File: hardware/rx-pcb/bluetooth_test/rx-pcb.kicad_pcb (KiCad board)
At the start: 4 copper layers, 23.1 x 37.6 mm, 36 parts, among them J1 Conn_01x05_Pin, J2 Conn_01x04_Pin, J3 Conn_Coaxial_Small, J4 Conn_01x04_Pin, J5 Conn_01x02_Pin, SW1 SW_SPST, U1 STM32WB05KZV6TR, U2 STS4L-AD1B-R3, U3 LMT70AYFQR, X1 Q22FA12800025, X2 ABS07-32.768KHZ-1-T

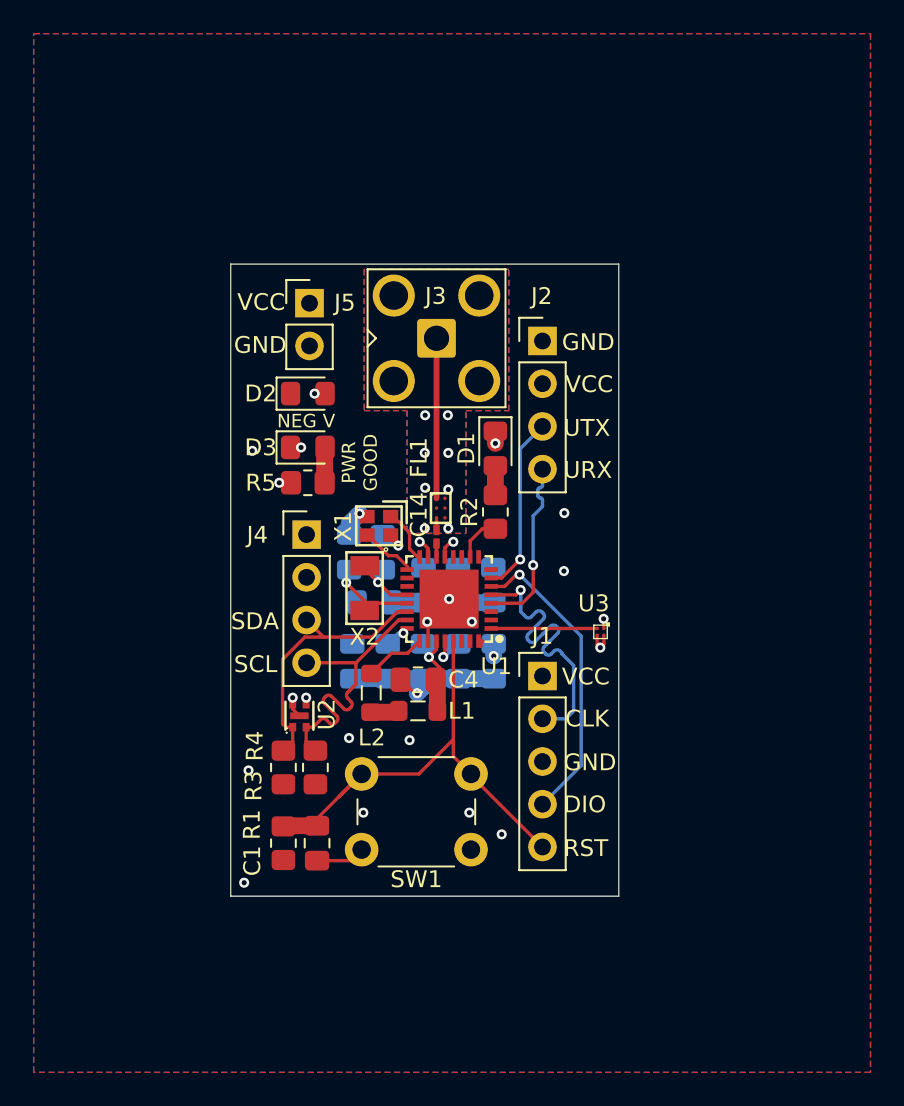
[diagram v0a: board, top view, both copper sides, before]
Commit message: backup of sensor-bluetooth board. re-wiring it.
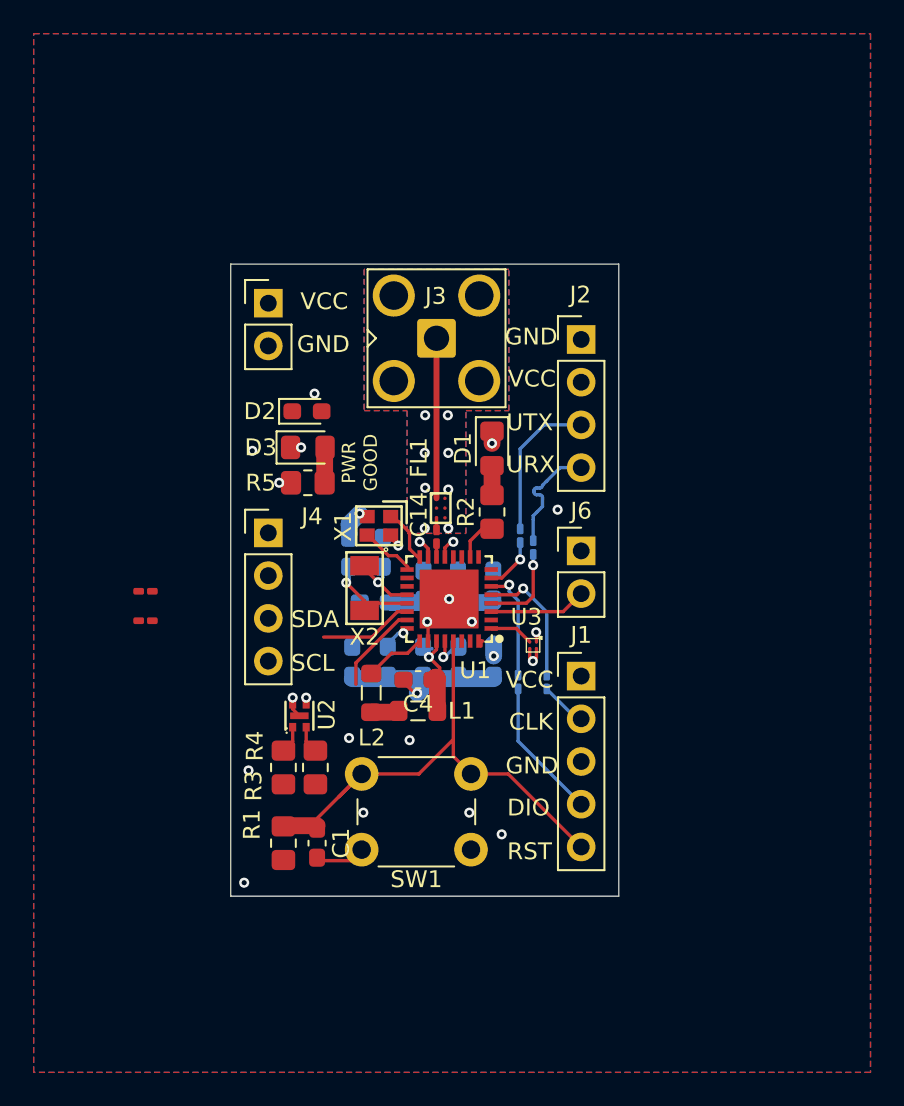
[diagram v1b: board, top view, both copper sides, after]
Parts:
- added J6: Conn_01x02_Pin, Connector_PinHeader_2.54mm:PinHeader_1x02_P2.54mm_Vertical, F.Cu at (163.1, 98.8)
- added R1: 0, Resistor_SMD:R_0201_0603Metric_Pad0.64x0.40mm_HandSolder, F.Cu at (137.2, 101.2)
- added R10: 0, Resistor_SMD:R_0201_0603Metric_Pad0.64x0.40mm_HandSolder, B.Cu at (160.2, 98.5)
- added R6: 0, Resistor_SMD:R_0201_0603Metric_Pad0.64x0.40mm_HandSolder, F.Cu at (137.2, 102.9)
- added R7: 0, Resistor_SMD:R_0201_0603Metric_Pad0.64x0.40mm_HandSolder, B.Cu at (159.4, 97.8)
- added R8: 0, Resistor_SMD:R_0201_0603Metric_Pad0.64x0.40mm_HandSolder, B.Cu at (159.3, 106.5)
- added R9: 0, Resistor_SMD:R_0201_0603Metric_Pad0.64x0.40mm_HandSolder, B.Cu at (161.0, 106.5)
- C1, C10, C11, C12, C13, C2, C3, C4, C5, C6, C7, C8, C9: footprint rx-parts:C_0805_2012Metric_Pad1.18x1.45mm_HandSolder -> Capacitor_SMD:C_0603_1608Metric_Pad1.08x0.95mm_HandSolder
- D2: value LED -> D_Zener; footprint rx-parts:LED_0805_2012Metric_Pad1.15x1.40mm_HandSolder -> Diode_SMD:D_0603_1608Metric_Pad1.05x0.95mm_HandSolder
- R3, R4: value 100k -> 50k
- moved U3 4.09 mm to (160.2, 104.4)
- moved J5 2.45 mm to (144.4, 84.0)
- moved J2 2.30 mm to (163.1, 86.2)
- moved J1 2.30 mm to (163.1, 106.2)
- moved J4 2.28 mm to (144.4, 97.7)
- moved D2 1.05 mm to (146.8, 90.5)
- moved D1 0.20 mm to (157.8, 92.7)
- moved R2 0.20 mm to (157.8, 96.4)
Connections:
- U1 pad 22: /i2c_sda -> Net-(U1-PB7)
- U1 pad 23: /i2c_scl -> Net-(U1-PB6)
- U1 pad 3: unconnected-(U1-PB1-Pad3) -> /ADC_jump
- U1 pad 4: /uart_rx -> Net-(U1-PB0)
- U1 pad 5: /swclk -> Net-(U1-PA3)
- U1 pad 6: /swdio -> Net-(U1-PA2)
- U1 pad 7: /uart_tx -> Net-(U1-PA1)
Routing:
- net /i2c_scl: track 17.6 -> 1.62 mm
- net /swclk: track 18.0 -> 2.78 mm, vias 1 -> 0
- net /i2c_sda: track 16.2 -> 1.62 mm
- net /swdio: track 18.1 -> 8.41 mm, vias 1 -> 0
- net Net-(U1-PA3): track 0.00 -> 7.79 mm, vias 0 -> 1
- net Net-(U1-PA2): track 0.00 -> 6.72 mm, vias 0 -> 1
- net /ADC_jump: track 0.00 -> 5.79 mm
- net Net-(U1-PB7): track 0.00 -> 5.59 mm
- net Net-(U1-PB6): track 0.00 -> 5.37 mm
- net Net-(U1-PB0): track 0.00 -> 5.17 mm, vias 0 -> 1
- net /TMP_A: track 6.30 -> 2.62 mm
- net /uart_rx: track 10.6 -> 6.97 mm, vias 1 -> 0
- net Net-(U1-PA1): track 0.00 -> 3.18 mm, vias 0 -> 1
- net /rst: track 29.0 -> 31.3 mm
- net /uart_tx: track 10.6 -> 8.98 mm, vias 1 -> 0
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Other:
- board text removed: "NEG V"

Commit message: updated rx-board with compartmentalization resistors, updated silkscreen
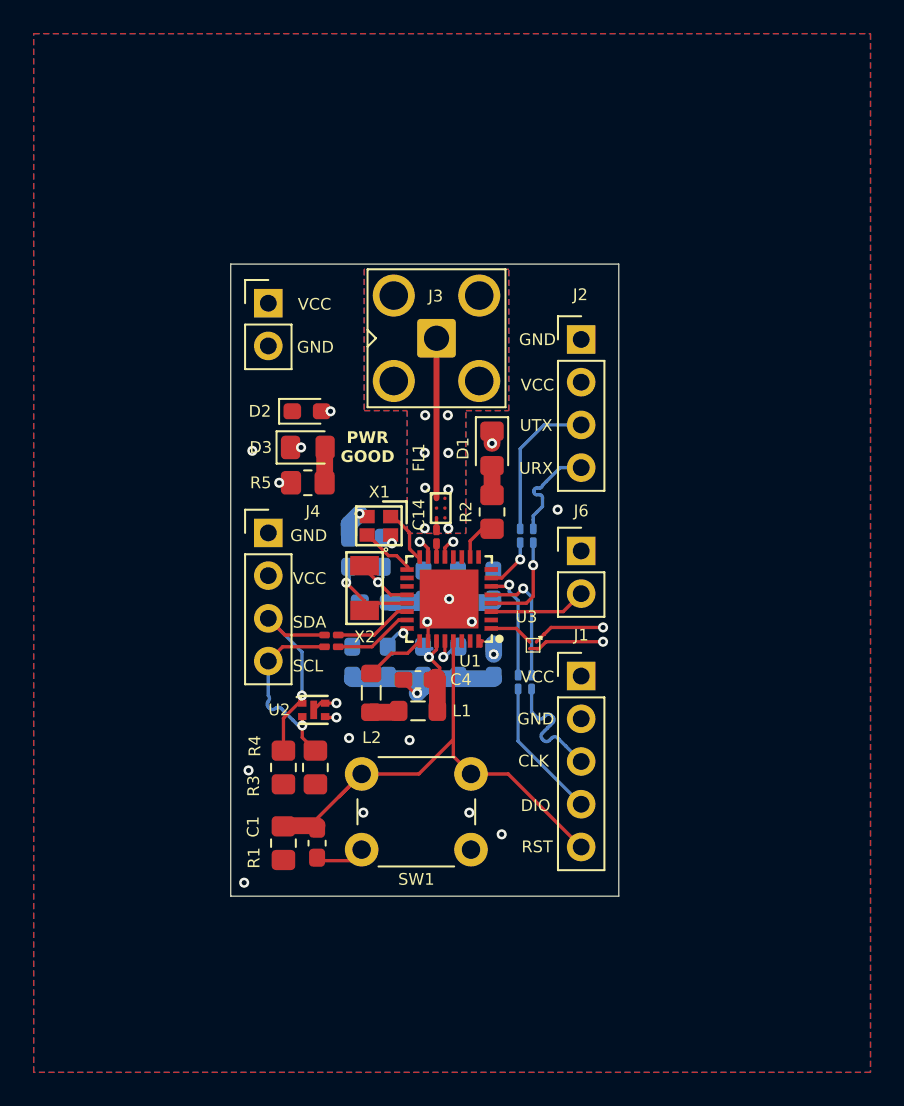
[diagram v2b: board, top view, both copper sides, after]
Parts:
- moved R1 11.5 mm to (148.2, 104.5), turned to 180 degrees
- moved R6 11.1 mm to (148.2, 103.8)
- moved U2 0.92 mm to (147.2, 108.2), turned to 0 degrees
- moved R9 0.90 mm to (160.1, 106.5)
- moved R10 0.70 mm to (160.2, 97.8)
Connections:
- J1 pad 2: /swclk -> GND
- J1 pad 3: GND -> /swclk
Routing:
- net /i2c_sda: track 1.62 -> 13.0 mm, vias 0 -> 1
- net /i2c_scl: track 1.62 -> 11.4 mm, vias 0 -> 1
- net /swclk: track 2.78 -> 7.62 mm
- net GND: track 26.1 -> 30.5 mm
- net VCC: track 6.78 -> 10.4 mm
- net Net-(U1-PB7): track 5.59 -> 4.67 mm
- net Net-(U1-PB0): track 5.17 -> 5.87 mm
- net /uart_rx: track 6.97 -> 6.27 mm
- net Net-(U1-PB6): track 5.37 -> 4.75 mm

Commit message: updates for dr weeks
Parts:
- removed D3: LED, rx-parts:LED_0805_2012Metric_Pad1.15x1.40mm_HandSolder
- removed J6: Conn_01x02_Pin, Connector_PinHeader_2.54mm:PinHeader_1x02_P2.54mm_Vertical
- removed the R1 at (148.2, 104.5)
- removed the R1 at (145.3, 116.1)
- removed R5: 10k, rx-parts:R_0805_2012Metric_Pad1.20x1.40mm_HandSolder
- added R1: 0, Resistor_SMD:R_0805_2012Metric_Pad1.20x1.40mm_HandSolder, F.Cu at (164.0, 97.2)
- C1, C4: footprint Capacitor_SMD:C_0603_1608Metric_Pad1.08x0.95mm_HandSolder -> Capacitor_SMD:C_0805_2012Metric_Pad1.18x1.45mm_HandSolder; moved to B.Cu
- C10, C11, C12, C13, C2, C3, C5, C6, C7, C8, C9: footprint Capacitor_SMD:C_0603_1608Metric_Pad1.08x0.95mm_HandSolder -> Capacitor_SMD:C_0805_2012Metric_Pad1.18x1.45mm_HandSolder
- D2, R3, R4: moved to B.Cu
- J3: footprint rx-parts:SMA_Amphenol_901-143_Horizontal -> Connector_Coaxial:SMA_Samtec_SMA-J-P-H-ST-EM1_EdgeMount
- R10, R7, R8, R9: moved to F.Cu
- R6: footprint Resistor_SMD:R_0201_0603Metric_Pad0.64x0.40mm_HandSolder -> Resistor_SMD:R_0805_2012Metric_Pad1.20x1.40mm_HandSolder
- U3: value LMT70AYFQR -> STS4L-AD1B-R3; footprint rx-parts:DSBGA-4_L0.8-W0.8-R2-C2-P0.40-BL -> rx-parts:DFN-4_L1.5-W1.5-P0.80-TL-EP
- moved J2 33.1 mm to (143.2, 112.7), turned to 180 degrees
- moved SW1 31.4 mm to (150.2, 85.7), turned to 0 degrees
- moved C1 28.6 mm to (151.9, 87.9), turned to 90 degrees
- moved R4 28.2 mm to (162.7, 89.4)
- moved U2 27.4 mm to (168.0, 90.4)
- moved J3 26.9 mm to (160.0, 112.4), turned to -90 degrees
- moved J4 26.1 mm to (167.8, 86.0), turned to -90 degrees
- moved R3 25.7 mm to (160.2, 89.4)
- moved J1 24.8 mm to (143.2, 91.4)
- moved D1 19.7 mm to (154.6, 112.1), turned to 90 degrees
- moved R6 19.1 mm to (166.1, 97.2), turned to -90 degrees
- moved C3 17.3 mm to (166.5, 100.2)
- moved C2 16.2 mm to (166.2, 105.0), turned to -90 degrees
- moved C11 15.9 mm to (163.5, 98.0), turned to 0 degrees
- moved X2 15.6 mm to (165.7, 102.6), turned to 90 degrees
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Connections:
- U1 pad 3: /ADC_jump -> unconnected-(U1-PB1-Pad3)
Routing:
- net /i2c_scl: track 11.4 -> 21.0 mm, vias 1 -> 4
- net GND: track 30.5 -> 22.8 mm, vias 22 -> 38
- net /rst: track 31.3 -> 38.1 mm, vias 0 -> 1
- net /ANT: track 9.52 -> 3.38 mm
- net VCC: track 10.4 -> 4.60 mm, vias 13 -> 16
- net /ADC_jump: track 5.79 -> 0.00 mm
- net /i2c_sda: track 13.0 -> 17.0 mm, vias 1 -> 0
- net /swclk: track 7.62 -> 11.2 mm
- net /uart_rx: track 6.27 -> 9.77 mm
- net Net-(U1-PA3): track 7.42 -> 4.15 mm, vias 1 -> 0
- net Net-(U1-PA2): track 6.72 -> 3.82 mm, vias 1 -> 0
- net /TMP_A: track 2.62 -> 0.00 mm
- net /swdio: track 8.41 -> 10.8 mm
- net /vlxsd: track 3.68 -> 1.47 mm
- net Net-(D3-A): track 2.11 -> 0.00 mm
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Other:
- board size 23.1 x 37.6 mm -> 28.2 x 30.3 mm
- board text added: "+"
- board text added: "-"
- board text added: "clk"
- board text added: "dio"
- board text added: "rst"
- board text added: "rx"
- board text added: "sda"
- board text added: "tx"
- board text removed: "CLK"
- board text removed: "DIO"
- board text removed: "GND"
- board text removed: "PWR GOOD"
- board text removed: "RST"
- board text removed: "SCL"
- board text removed: "SDA"
- board text removed: "URX"
- board text removed: "UTX"
- board text removed: "VCC"
- board text removed: "trace impedance based upon: JLC04161H-7628(Standard/Finished thickness1.59mm±10%)"

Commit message: updated PCB for weeks purchase
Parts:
- removed J5: Conn_01x02_Pin, Connector_PinHeader_2.54mm:PinHeader_1x02_P2.54mm_Vertical
- added J6: Conn_01x03_Pin, Connector_PinHeader_2.54mm:PinHeader_1x03_P2.54mm_Vertical, F.Cu at (146.0, 86.0)
- C14: footprint Capacitor_SMD:C_0201_0603Metric_Pad0.64x0.40mm_HandSolder -> rx-parts:R_0201_0603Metric_Pad0.64x0.40mm_HandSolder_correctedclearance
- R10, R7, R8, R9: footprint Resistor_SMD:R_0201_0603Metric_Pad0.64x0.40mm_HandSolder -> Resistor_SMD:R_0805_2012Metric
- moved R7 4.51 mm to (148.4, 105.4)
- moved R8 4.50 mm to (148.4, 102.5)
- moved D1 4.41 mm to (152.6, 108.2), turned to -90 degrees
- moved J1 2.76 mm to (140.9, 89.8)
- moved J2 2.71 mm to (140.9, 111.2)
- moved J3 1.49 mm to (159.9, 110.9)
- moved D2 1.20 mm to (143.4, 89.1), turned to 90 degrees
- moved R10 1.04 mm to (151.9, 103.9)
- moved R9 1.04 mm to (151.9, 101.1)
- moved FL1 0.24 mm to (159.8, 108.2)
- moved C14 0.19 mm to (160.0, 106.3)
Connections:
- U1 pad 2: unconnected-(U1-PB2-Pad2) -> /Pg
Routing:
- net /Pg: track 0.00 -> 22.2 mm
- net Net-(U1-PA1): track 4.14 -> 8.08 mm
- net Net-(U1-PA2): track 3.82 -> 7.75 mm
- net /uart_tx: track 10.2 -> 7.21 mm
- net /swdio: track 10.8 -> 9.01 mm
- net /rst: track 38.1 -> 39.8 mm
- net /swclk: track 11.2 -> 12.7 mm
- net /ANT: track 3.38 -> 2.18 mm
- net VCC: track 4.60 -> 5.28 mm, vias 16 -> 18
- net Net-(U1-PA3): track 4.15 -> 4.82 mm
- net /uart_rx: track 9.77 -> 10.3 mm
- net GND: track 22.8 -> 22.3 mm, vias 38 -> 43
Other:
- board size 28.2 x 30.3 mm -> 30.5 x 28.8 mm
